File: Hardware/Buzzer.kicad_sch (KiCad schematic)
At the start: 6 parts, among them J6 BuzzConn, Q3 PSMN8R5-40MSDX

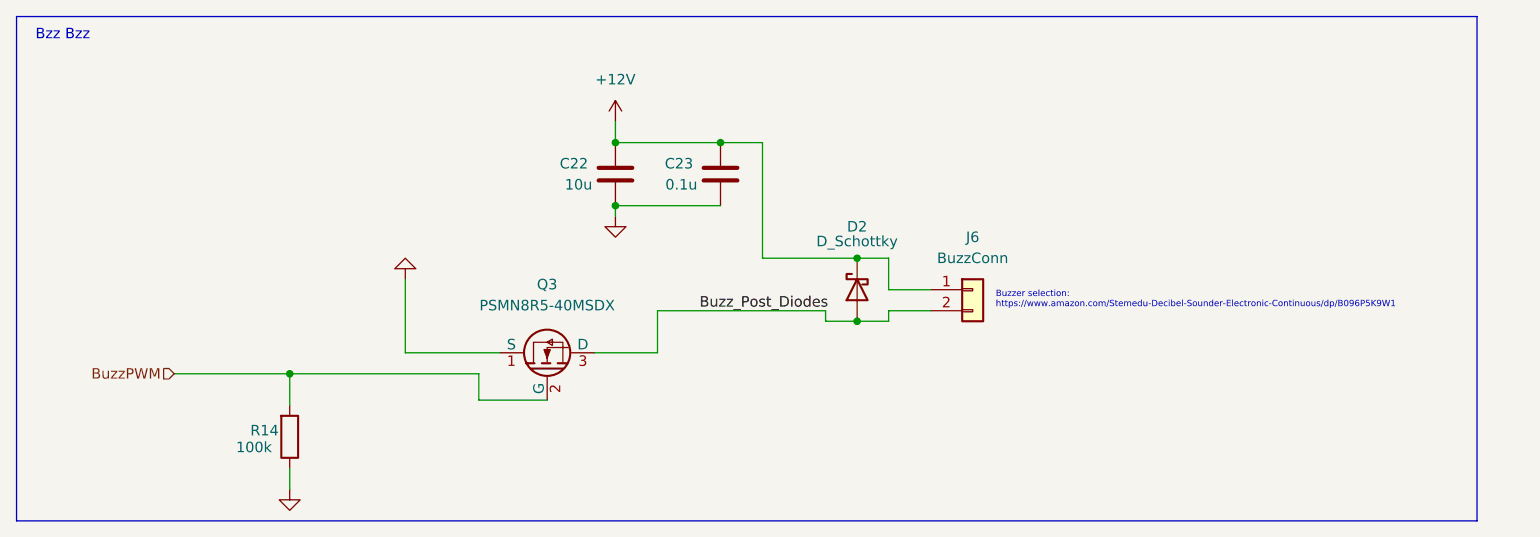
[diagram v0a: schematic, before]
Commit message: Bring Hardware folder from RevB
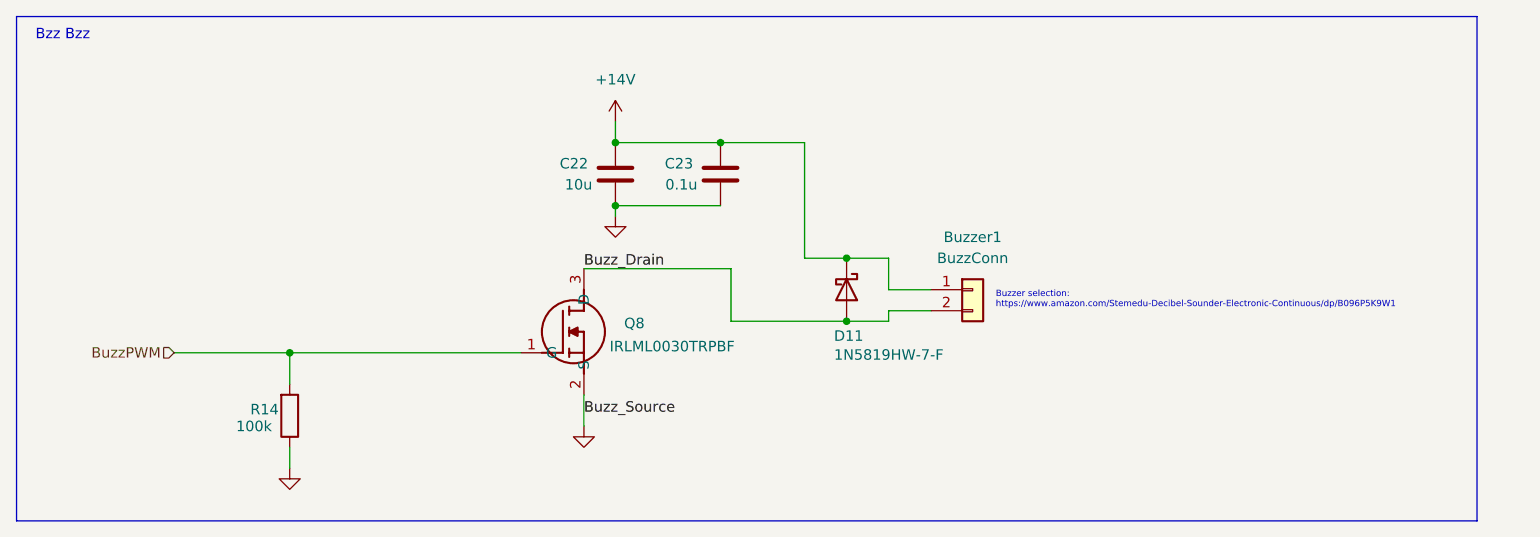
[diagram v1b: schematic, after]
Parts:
- removed D2: D_Schottky, SK32A_LTP:SDO_DO-214AC-SMA_MCE, symbol Device:D_Schottky
- removed Q3: PSMN8R5-40MSDX, UTSVT_Power:PSMN8R5-40MSDX, symbol utsvt_power:PSMN8R5-40MSDX
- added D11: 1N5819HW-7-F, charger_parts:1N5819HW-7-F, symbol Device:D_Schottky
- added Q8: IRLML0030TRPBF, charger_parts:IRLML0030TRPBF, symbol IRLML0030TRPBF:IRLML0030TRPBF
- Buzzer1: renamed from J6; footprint 153091202:1053091202 -> UTSVT_Connectors:Molex_Nano-Fit_105309-xx02_1x02_P2.50mm_Vertical; P/N 1053091202 -> 105309-1202
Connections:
- net BuzzPWM: now also Q8.1 (G)
- net GND: now also Q8.2 (S)
- net +12V renamed +14V
- net +14V: now also D11.1 (K)
- net Buzz_Post_Diodes renamed Buzz_Drain
- net Buzz_Drain: now also D11.2 (A), Q8.3 (D)
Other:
- moved on the sheet: R14
